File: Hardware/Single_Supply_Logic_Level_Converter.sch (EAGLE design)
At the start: 31 parts, among them U1 TXB0104, U2 TPS61200, U3 ADJ

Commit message: updated version number
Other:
- note added: "v10"
- note removed: "v01"
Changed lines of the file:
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@@
 <plain>
 <text x="167.64" y="10.16" size="2.54" layer="94" font="vector">Mary West</text>
-<text x="238.76" y="7.62" size="2.54" layer="94" font="vector">v01</text>
+<text x="238.76" y="7.62" size="2.54" layer="94" font="vector">v10</text>
 <text x="116.84" y="167.64" size="2.032" layer="97" font="vector" ratio="15">VIN: 3 - 5.5V</text>
 <wire x1="0" y1="96.52" x2="111.76" y2="96.52" width="0.1524" layer="97" style="shortdash"/>

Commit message: Updates per Engineering Design Review
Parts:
- removed FD3: FIDUCIALUFIDUCIAL, SparkFun-Aesthetics:FIDUCIALUFIDUCIAL
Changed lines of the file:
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@@
 <part name="FD1" library="SparkFun-Aesthetics" deviceset="FIDUCIAL" device="UFIDUCIAL"/>
 <part name="FD2" library="SparkFun-Aesthetics" deviceset="FIDUCIAL" device="UFIDUCIAL"/>
-<part name="FD3" library="SparkFun-Aesthetics" deviceset="FIDUCIAL" device="UFIDUCIAL"/>
 <part name="FD4" library="SparkFun-Aesthetics" deviceset="FIDUCIAL" device="UFIDUCIAL"/>
 <part name="C7" library="SparkFun-Capacitors" deviceset="10UF-POLAR" device="-EIA3216-16V-10%(TANT)" value="10uF"/>
@@
 <instance part="FD1" gate="G$1" x="213.36" y="25.4"/>
 <instance part="FD2" gate="G$1" x="218.44" y="25.4"/>
-<instance part="FD3" gate="G$1" x="223.52" y="25.4"/>
 <instance part="FD4" gate="G$1" x="228.6" y="25.4"/>
 <instance part="C7" gate="G$1" x="86.36" y="127"/>

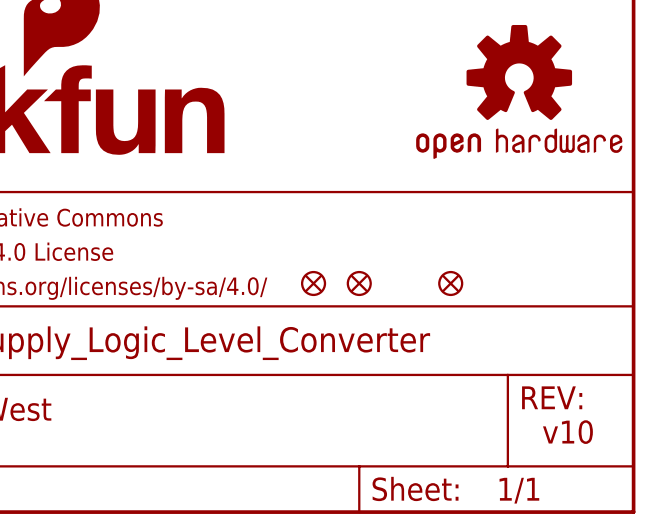
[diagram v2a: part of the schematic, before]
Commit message: Adding a lost fiducial
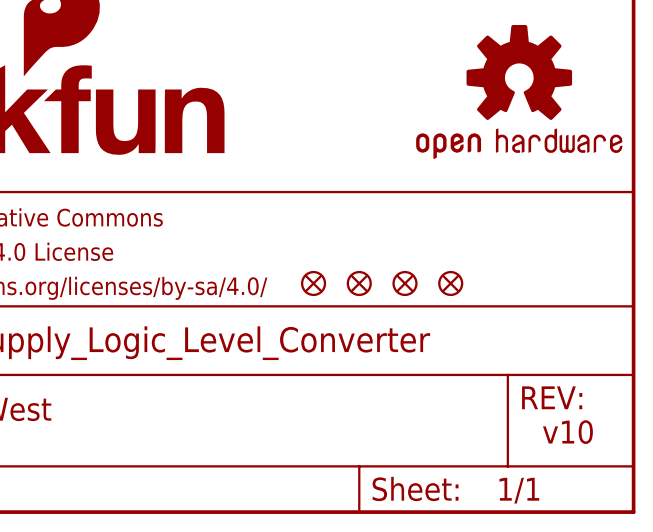
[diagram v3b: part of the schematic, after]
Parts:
- added FD3: FIDUCIALUFIDUCIAL, SparkFun-Aesthetics:FIDUCIALUFIDUCIAL
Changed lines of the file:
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@@
 <part name="J4" library="SparkFun-Connectors" deviceset="CONN_01" device=""/>
 <part name="GND15" library="SparkFun" deviceset="GND" device=""/>
+<part name="FD3" library="SparkFun-Aesthetics" deviceset="FIDUCIAL" device="UFIDUCIAL"/>
 </parts>
 <sheets>
@@
 <instance part="J4" gate="G$1" x="154.94" y="55.88"/>
 <instance part="GND15" gate="1" x="167.64" y="50.8"/>
+<instance part="FD3" gate="G$1" x="223.52" y="25.4"/>
 </instances>
 <busses>

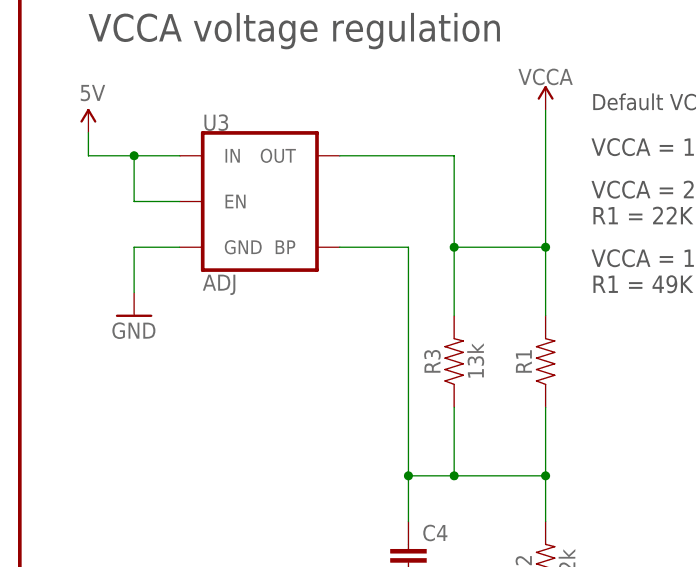
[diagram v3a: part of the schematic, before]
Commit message: updated MIC5205(ADJ) part
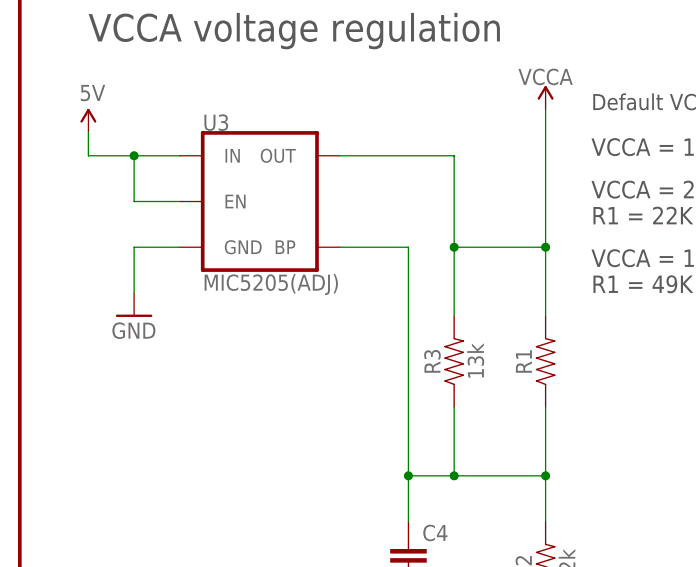
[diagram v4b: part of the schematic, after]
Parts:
- U3: value ADJ -> MIC5205(ADJ)
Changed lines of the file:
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@@
 <part name="LOGO1" library="SparkFun-Aesthetics" deviceset="SFE_LOGO_NAME_FLAME" device=".1_INCH" value="SFE_LOGO_NAME_FLAME.1_INCH"/>
 <part name="SUPPLY12" library="SparkFun-Aesthetics" deviceset="5V" device=""/>
-<part name="U3" library="SparkFun-IC-Power" deviceset="V_REG_MIC5205" device="ADJ" value="ADJ"/>
+<part name="U3" library="SparkFun-IC-Power" deviceset="V_REG_MIC5205" device="ADJ" value="MIC5205(ADJ)"/>
 <part name="GND1" library="SparkFun" deviceset="GND" device=""/>
 <part name="R3" library="SparkFun-Resistors" deviceset="13KOHM" device="-0603-1/10W-1%" value="13k"/>
